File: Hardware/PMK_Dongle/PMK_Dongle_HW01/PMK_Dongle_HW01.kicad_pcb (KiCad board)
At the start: 4 copper layers, 10.4 x 15.4 mm, 37 parts, among them IC1 ESP32-S2FH4, J1 USB_A, U1 MIC5528-3.3YMT-T5, Y1 Crystal_GND24_Small

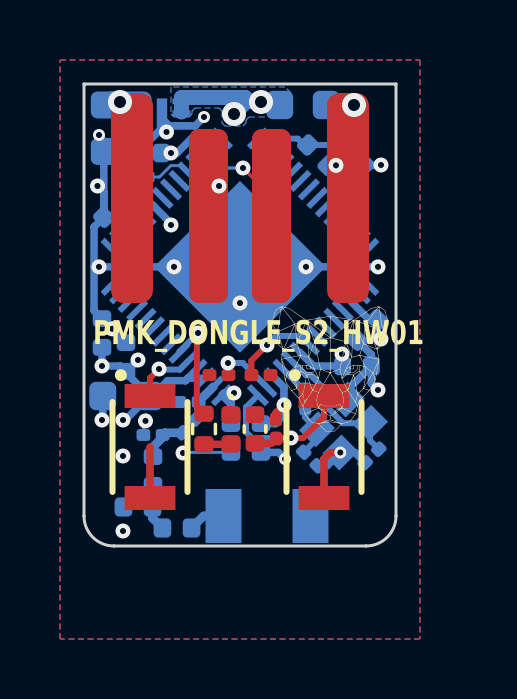
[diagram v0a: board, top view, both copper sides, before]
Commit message: fixed hole size for order
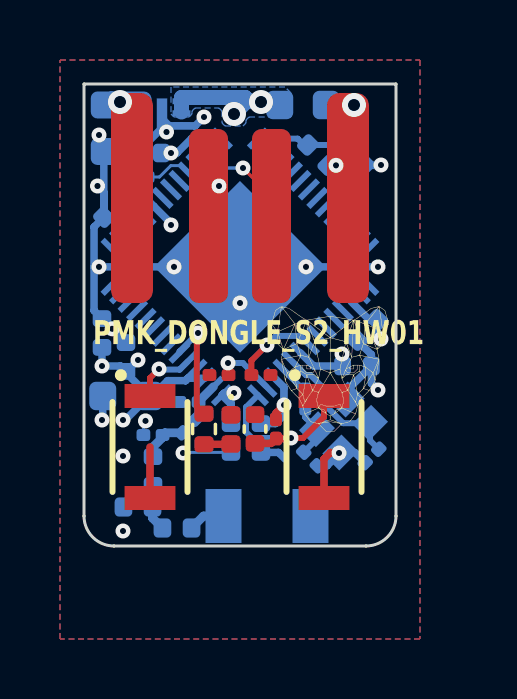
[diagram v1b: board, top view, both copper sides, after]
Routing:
- net GND: track 46.6 -> 46.7 mm, vias 21 -> 20
